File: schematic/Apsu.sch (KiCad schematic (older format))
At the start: 45 parts

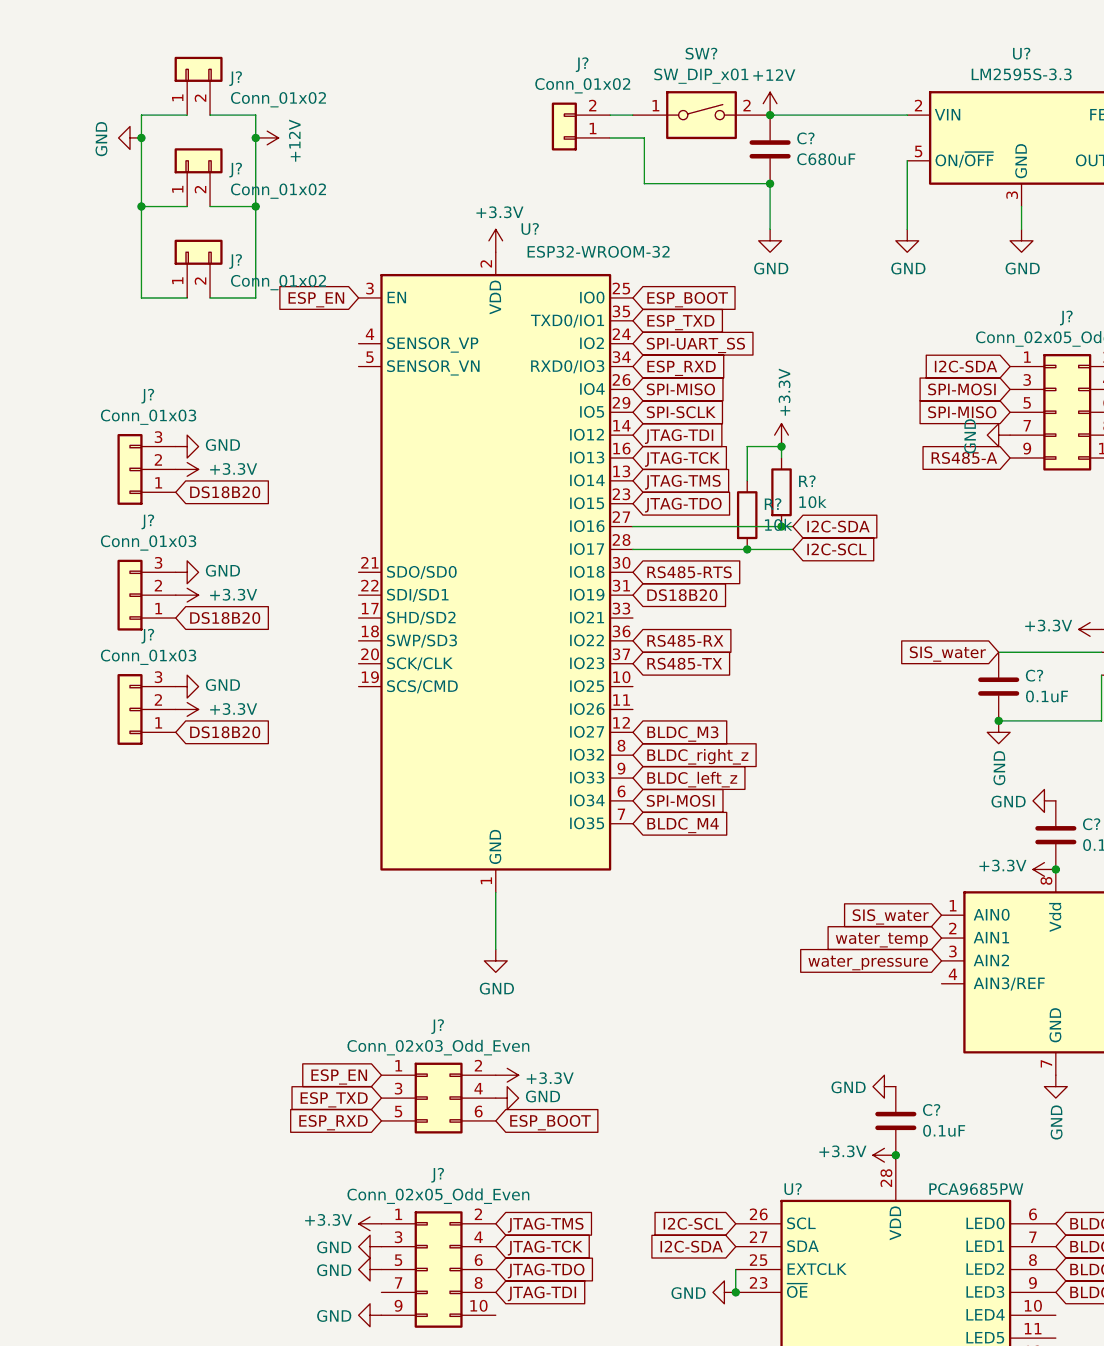
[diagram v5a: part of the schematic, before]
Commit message: voltage divider
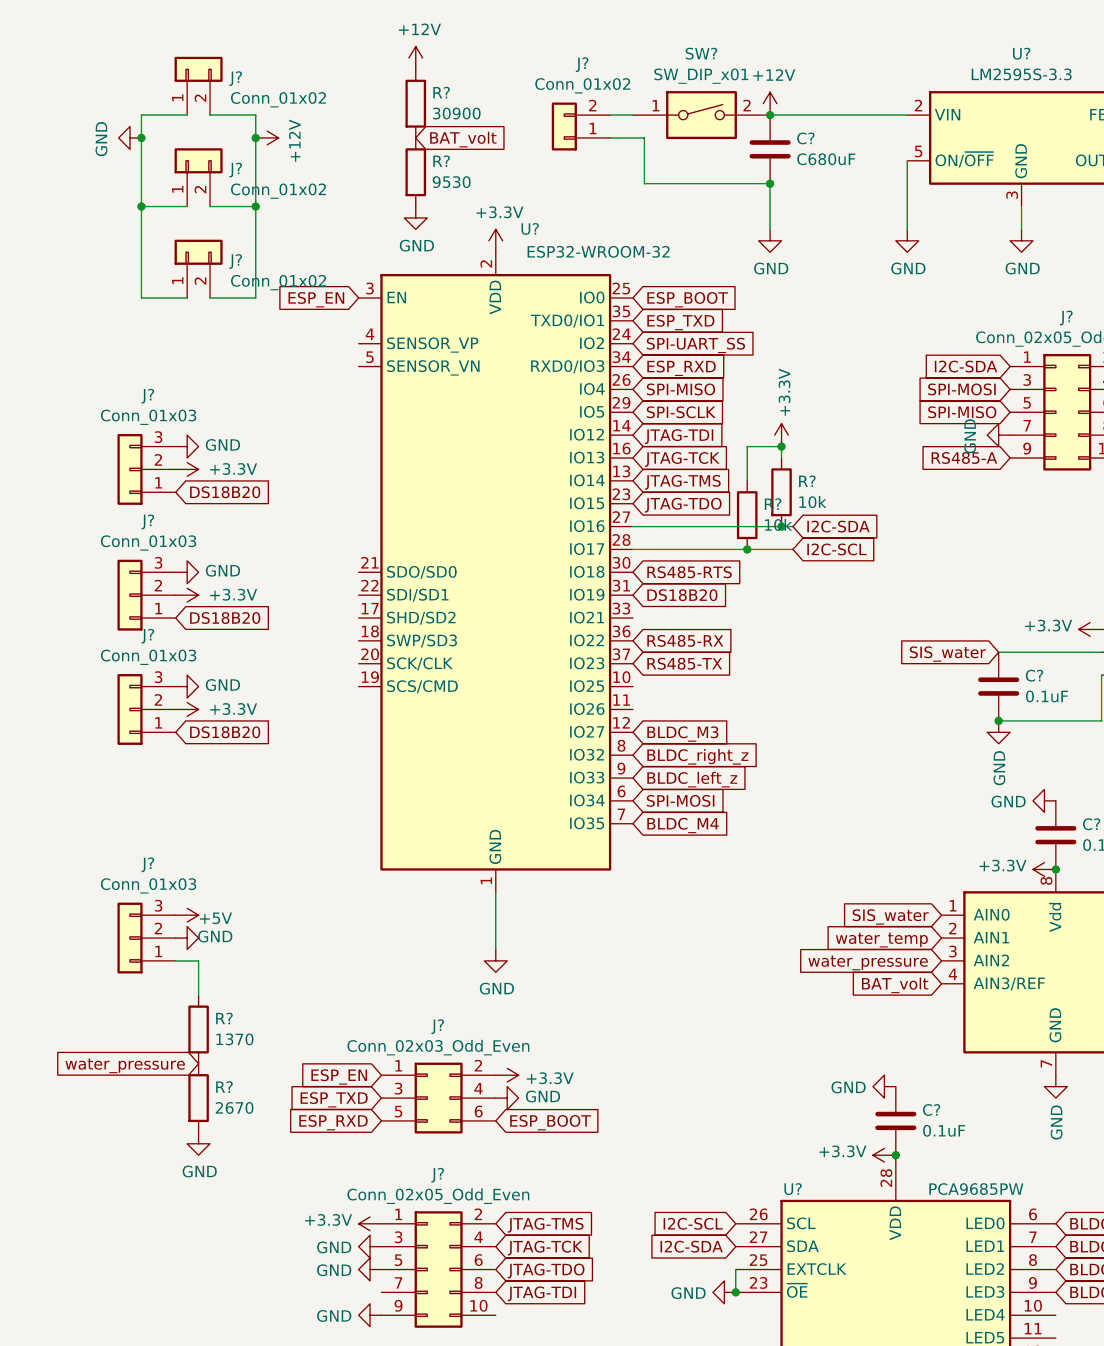
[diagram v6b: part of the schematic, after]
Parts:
- added J?: Conn_01x03, symbol Connector_Generic:Conn_01x03
- added R?: 30900, symbol Device:R
- added R?: 9530, symbol Device:R
- added R?: 1370, symbol Device:R
- added R?: 2670, symbol Device:R
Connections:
- net +12V: now also R?.1
- net +5V: now also J?.3 (Pin_3)
- net GND: now also J?.2 (Pin_2), R?.2, R?.2
- net water_pressure: now also R?.1, R?.2
- net BAT_volt: now reaches U?.4 (AIN3/REF)
- net BAT_volt: now also R?.1, R?.2
- new net: J?.1 (Pin_1), R?.1
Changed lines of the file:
@@
 	0    -1   -1   0
 $EndComp
+$Comp
+L Connector_Generic:Conn_01x03 J?
+U 1 1 5ECD4049
+P 800 4550
+F 0 "J?" H 718 4225 50  0000 C CNN
+F 1 "Conn_01x03" H 718 4316 50  0000 C CNN
+F 2 "" H 800 4550 50  0001 C CNN
+F 3 "~" H 800 4550 50  0001 C CNN
+	1    800  4550
+	-1   0    0    1
+$EndComp
+Text GLabel 1100 5100 0    50   Input ~ 0
+water_pressure
+$Comp
+L power:GND #PWR?
+U 1 1 5ECD62AA
+P 1000 4550
+F 0 "#PWR?" H 1000 4300 50  0001 C CNN
+F 1 "GND" V 1005 4377 50  0000 C CNN
+F 2 "" H 1000 4550 50  0001 C CNN
+F 3 "" H 1000 4550 50  0001 C CNN
+	1    1000 4550
+	0    -1   -1   0
+$EndComp
+$Comp
+L power:+5V #PWR?
+U 1 1 5ECD89BE
+P 1000 4450
+F 0 "#PWR?" H 1000 4300 50  0001 C CNN
+F 1 "+5V" V 1015 4623 50  0000 C CNN
+F 2 "" H 1000 4450 50  0001 C CNN
+F 3 "" H 1000 4450 50  0001 C CNN
+	1    1000 4450
+	0    1    1    0
+$EndComp
+$Comp
+L power:+12V #PWR?
+U 1 1 5ED065A9
+P 2050 750
+F 0 "#PWR?" H 2050 600 50  0001 C CNN
+F 1 "+12V" H 2065 923 50  0000 C CNN
+F 2 "" H 2050 750 50  0001 C CNN
+F 3 "" H 2050 750 50  0001 C CNN
+	1    2050 750
+	1    0    0    -1
+$EndComp
+$Comp
+L power:GND #PWR?
+U 1 1 5ED06DB3
+P 2050 1350
+F 0 "#PWR?" H 2050 1100 50  0001 C CNN
+F 1 "GND" H 2055 1177 50  0000 C CNN
+F 2 "" H 2050 1350 50  0001 C CNN
+F 3 "" H 2050 1350 50  0001 C CNN
+	1    2050 1350
+	1    0    0    -1
+$EndComp
+$Comp
+L Device:R R?
+U 1 1 5ED077DC
+P 2050 900
+F 0 "R?" H 2120 946 50  0000 L CNN
+F 1 "30900" H 2120 855 50  0000 L CNN
+F 2 "" V 1980 900 50  0001 C CNN
+F 3 "~" H 2050 900 50  0001 C CNN
+	1    2050 900
+	1    0    0    -1
+$EndComp
+$Comp
+L Device:R R?
+U 1 1 5ED0AE8F
+P 2050 1200
+F 0 "R?" H 2120 1246 50  0000 L CNN
+F 1 "9530" H 2120 1155 50  0000 L CNN
+F 2 "" V 1980 1200 50  0001 C CNN
+F 3 "~" H 2050 1200 50  0001 C CNN
+	1    2050 1200
+	1    0    0    -1
+$EndComp
+Text GLabel 2050 1050 2    50   Input ~ 0
+BAT_volt
+Text GLabel 4350 4750 0    50   Input ~ 0
+BAT_volt
+$Comp
+L power:GND #PWR?
+U 1 1 5ED268B6
+P 1100 5400
+F 0 "#PWR?" H 1100 5150 50  0001 C CNN
+F 1 "GND" H 1105 5227 50  0000 C CNN
+F 2 "" H 1100 5400 50  0001 C CNN
+F 3 "" H 1100 5400 50  0001 C CNN
+	1    1100 5400
+	1    0    0    -1
+$EndComp
+$Comp
+L Device:R R?
+U 1 1 5ED268BC
+P 1100 4950
+F 0 "R?" H 1170 4996 50  0000 L CNN
+F 1 "1370" H 1170 4905 50  0000 L CNN
+F 2 "" V 1030 4950 50  0001 C CNN
+F 3 "~" H 1100 4950 50  0001 C CNN
+	1    1100 4950
+	1    0    0    -1
+$EndComp
+$Comp
+L Device:R R?
+U 1 1 5ED268C2
+P 1100 5250
+F 0 "R?" H 1170 5296 50  0000 L CNN
+F 1 "2670" H 1170 5205 50  0000 L CNN
+F 2 "" V 1030 5250 50  0001 C CNN
+F 3 "~" H 1100 5250 50  0001 C CNN
+	1    1100 5250
+	1    0    0    -1
+$EndComp
+Wire Wire Line
+	1000 4650 1100 4650
+Wire Wire Line
+	1100 4650 1100 4800
 $EndSCHEMATC

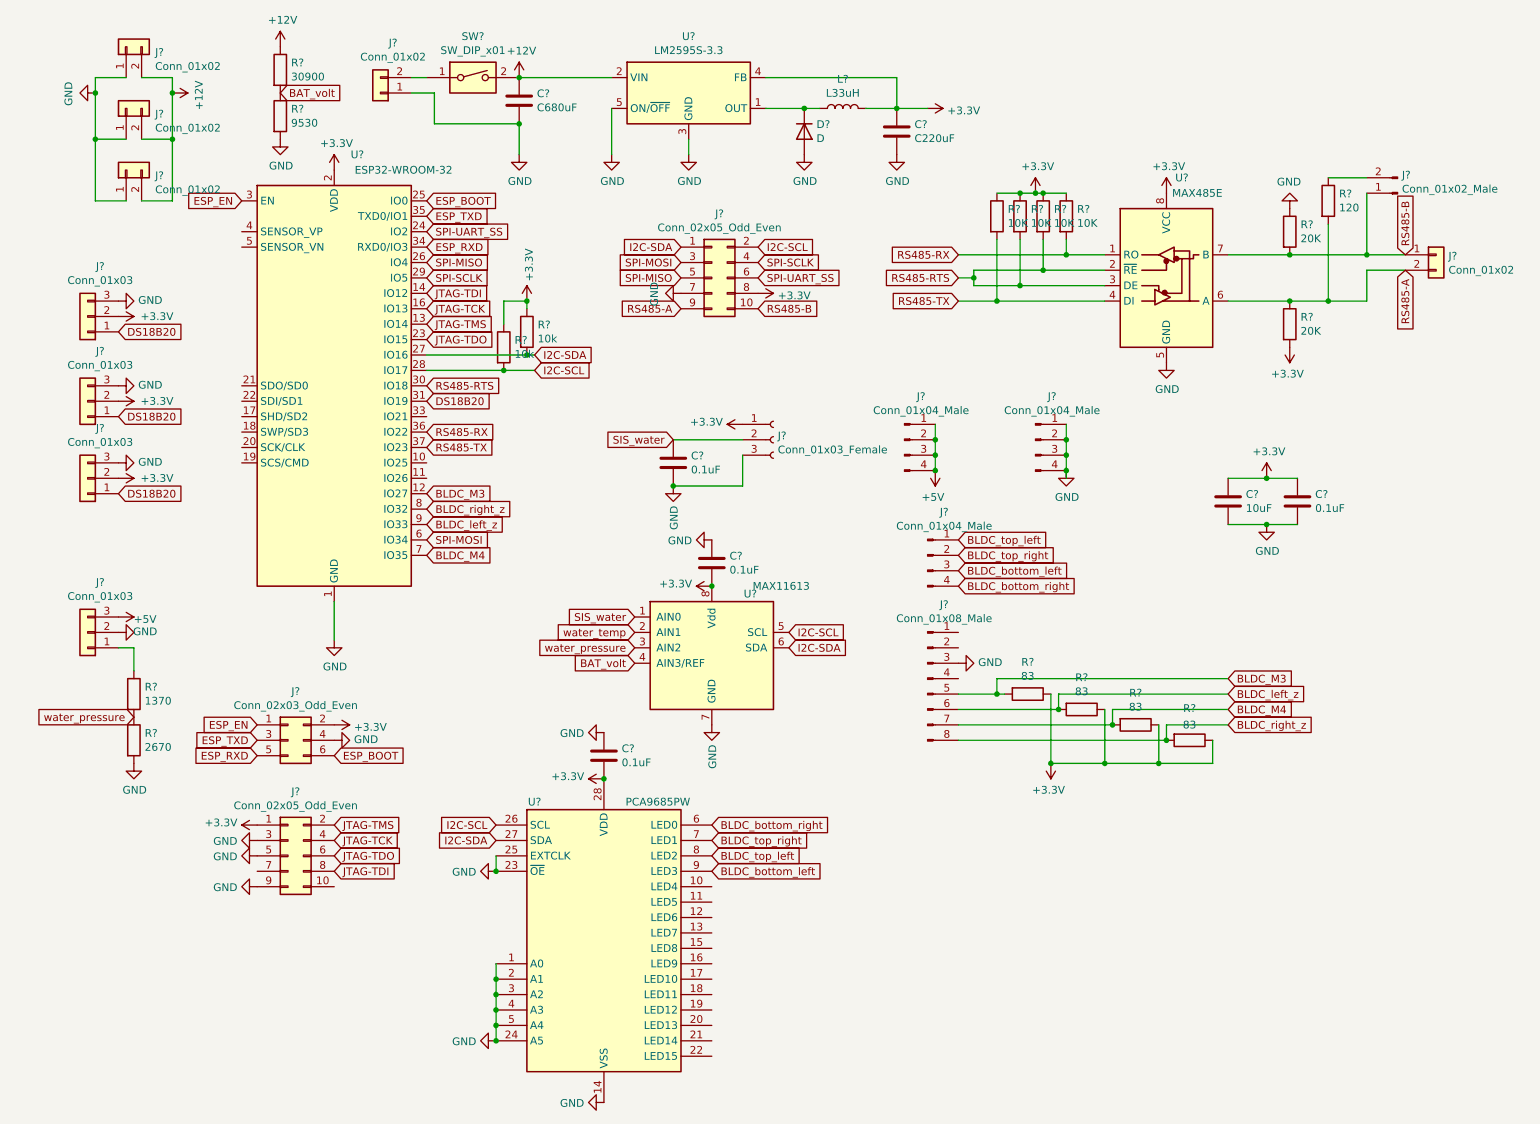
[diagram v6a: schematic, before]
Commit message: moved everything in seperated schematics
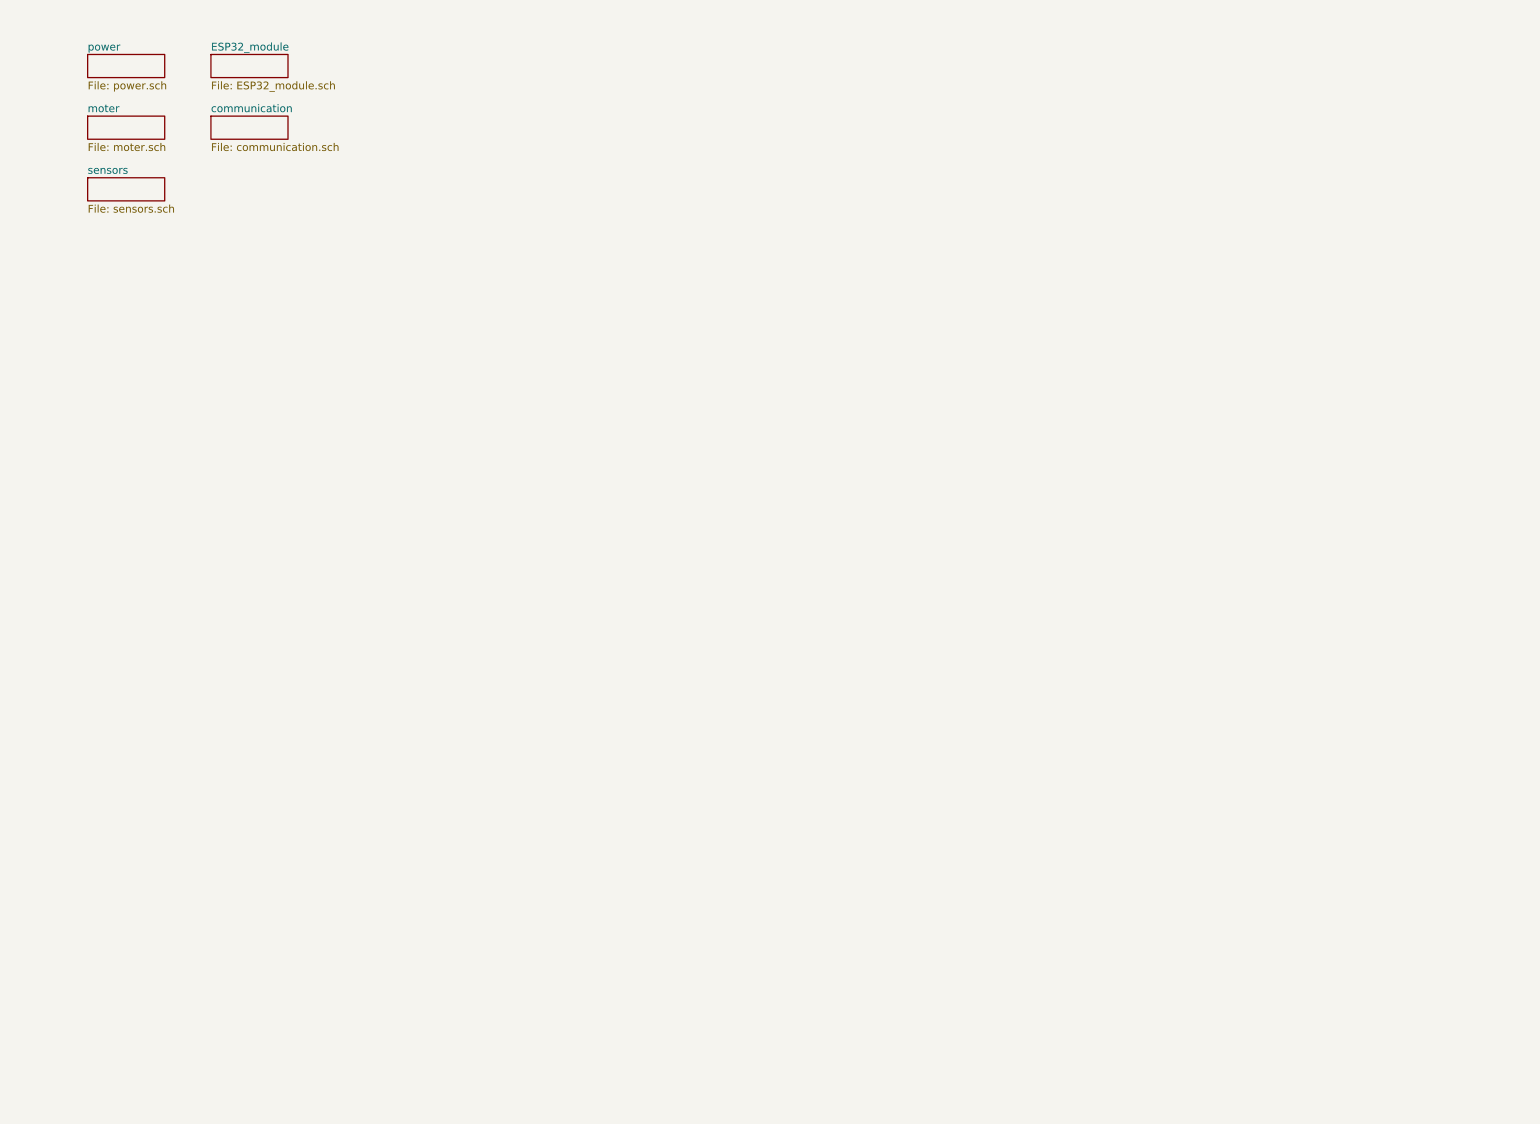
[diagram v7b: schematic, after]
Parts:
- removed C?: C220uF, symbol Device:C
- removed C?: C680uF, symbol Device:C
- removed C?: 10uF, symbol Device:C
- removed C? (x4): 0.1uF, symbol Device:C
- removed D?: D, symbol Device:D
- removed J?: Conn_02x03_Odd_Even, symbol Connector_Generic:Conn_02x03_Odd_Even
- removed J? (x5): Conn_01x02, symbol Connector_Generic:Conn_01x02
- removed J? (x2): Conn_02x05_Odd_Even, symbol Connector_Generic:Conn_02x05_Odd_Even
- removed J? (x3): Conn_01x04_Male, symbol Connector:Conn_01x04_Male
- removed J?: Conn_01x08_Male, symbol Connector:Conn_01x08_Male
- removed J?: Conn_01x03_Female, symbol Connector:Conn_01x03_Female
- removed J? (x4): Conn_01x03, symbol Connector_Generic:Conn_01x03
- removed J?: Conn_01x02_Male, symbol Connector:Conn_01x02_Male
- removed L?: L33uH, symbol Device:L
- removed R? (x2): 20K, symbol Device:R
- removed R?: 120, symbol Device:R
- removed R? (x4): 10K, symbol Device:R
- removed R? (x4): 83, symbol Device:R
- removed R? (x2): 10k, symbol Device:R
- removed R?: 30900, symbol Device:R
- removed R?: 9530, symbol Device:R
- removed R?: 1370, symbol Device:R
- removed R?: 2670, symbol Device:R
- removed SW?: SW_DIP_x01, symbol Switch:SW_DIP_x01
- removed U?: ESP32-WROOM-32, RF_Module:ESP32-WROOM-32, symbol RF_Module:ESP32-WROOM-32
- removed U?: LM2595S-3.3, Package_TO_SOT_SMD:TO-263-5_TabPin3, symbol Regulator_Switching:LM2595S-3.3
- removed U?: MAX11613, Package_SO:MSOP-8_3x3mm_P0.65mm, symbol Analog_ADC:MAX11613
- removed U?: MAX485E, symbol Interface_UART:MAX485E
- removed U?: PCA9685PW, Package_SO:TSSOP-28_4.4x9.7mm_P0.65mm, symbol Driver_LED:PCA9685PW

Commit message: power on seperate board
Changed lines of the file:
@@
 $Descr A4 11693 8268
 encoding utf-8
-Sheet 1 6
+Sheet 1 5
 Title ""
 Date ""
@@
 $EndSheet
 $Sheet
-S 800  800  500  150
-U 5EEC6D97
-F0 "power" 50
-F1 "power.sch" 50
-$EndSheet
-$Sheet
